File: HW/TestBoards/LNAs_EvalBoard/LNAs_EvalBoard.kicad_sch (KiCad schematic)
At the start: 13 parts, among them J1 SMA, J2 SMA, J3 Picoblade_2x1_H, J4 Picoblade_2x1_H, U1 HMC342, U2 BFHK-2582+, U3 HMC342

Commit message: LO1 Eval Board
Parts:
- removed J3, J4: Picoblade_2x1_H, Connector_Molex:Molex_PicoBlade_53261-0271_1x02-1MP_P1.25mm_Horizontal, symbol GGS_Connectors:Picoblade_2x1_H
- added H1, H2, H3, H4: M2.5, MountingHole:MountingHole_2.7mm_M2.5_Pad, symbol Mechanical:MountingHole_Pad
- added J3: Conn_01x04, Connector_PinSocket_2.00mm:PinSocket_1x04_P2.00mm_Vertical, symbol Connector_Generic:Conn_01x04
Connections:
- net GND: now also H1.1, H2.1, H3.1, H4.1, J3.2 (Pin_2), J3.4 (Pin_4)
- net VDD: now also J3.1 (Pin_1), J3.3 (Pin_3)
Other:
- moved on the sheet: J1, J2

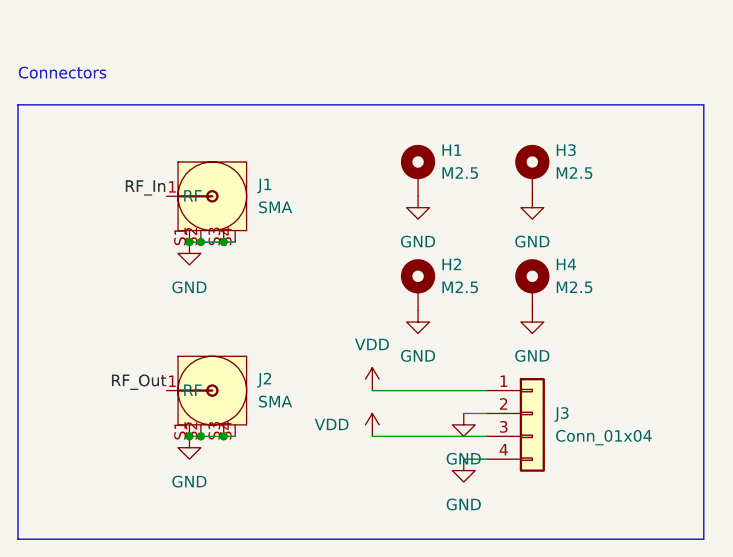
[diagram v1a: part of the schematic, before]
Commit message: Added Evaluation Boards for RO4003C 1.52 mm
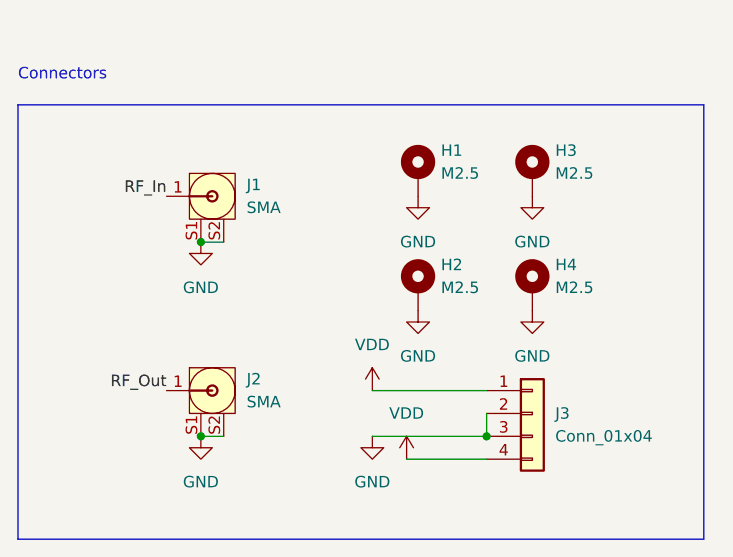
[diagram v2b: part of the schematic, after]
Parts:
- J1, J2: footprint GGS_Connectors:LINX_CONSMA020.062-G -> GGS_Connectors:Johnson_142-0761-861
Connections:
- net GND: now also J3.3 (Pin_3); no longer J1.S3, J1.S4, J2.S3, J2.S4, J3.4 (Pin_4)
- net VDD: now also J3.4 (Pin_4); no longer J3.3 (Pin_3)
